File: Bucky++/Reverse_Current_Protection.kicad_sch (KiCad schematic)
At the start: 32 parts, among them IC4 LTC4372CMS8#TRPBF, IC5 LTC4372CMS8#TRPBF, IC701 LTC4372CMS8#TRPBF, IC702 LTC4372CMS8#TRPBF, Q1 ISC016N04NM7V, Q2 ISC016N04NM7V, Q3 ISC016N04NM7V, Q4 ISC016N04NM7V, Q5 ISC016N04NM7V, Q6 ISC016N04NM7V, Q7 ISC016N04NM7V, Q8 ISC016N04NM7V

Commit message: fixed issues after Pedro's review
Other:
- note removed: "Control"
- note removed: "Reverse Current Protection"
- title: (none) -> Reverse_Current_Protection
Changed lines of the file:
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@@
 	(generator_version "9.0")
 	(paper "A4")
+	(title_block
+		(title "Reverse_Current_Protection")
+	)
 	(rectangle
-		(start 19.05 161.29)
-		(end 88.9 193.04)
+		(start 144.78 99.06)
+		(end 265.43 154.94)
 		(stroke
-			(width 0)
+			(width 1)
+			(type default)
+			(color 200 200 200 1)
+		)
+		(fill
+			(type none)
+		)
+	)
+	(rectangle
+		(start 17.78 160.02)
+		(end 92.71 193.04)
+		(stroke
+			(width 1)
 			(type default)
+			(color 200 200 200 1)
 		)
 		(fill
@@
 		)
 	)
-	(text "Control\n"
+	(rectangle
+		(start 144.78 35.56)
+		(end 265.43 95.25)
+		(stroke
+			(width 1)
+			(type default)
+			(color 200 200 200 1)
+		)
+		(fill
+			(type none)
+		)
+	)
+	(rectangle
+		(start 17.78 35.56)
+		(end 138.43 95.25)
+		(stroke
+			(width 1)
+			(type default)
+			(color 200 200 200 1)
+		)
+		(fill
+			(type none)
+		)
+	)
+	(rectangle
+		(start 17.78 99.06)
+		(end 138.43 154.94)
+		(stroke
+			(width 1)
+			(type default)
+			(color 200 200 200 1)
+		)
+		(fill
+			(type none)
+		)
+	)
+	(text_box "DESIGN NOTE:\nTVS diodes are added to protect the chip and MOSFETS\n"
 		(exclude_from_sim no)
-		(at 29.21 166.116 0)
+		(at 17.78 22.86 0)
+		(size 36.83 10.16)
+		(margins 1.3525 1.3525 1.3525 1.3525)
+		(stroke
+			(width 0.8)
+			(type solid)
+			(color 200 200 200 1)
+		)
+		(fill
+			(type none)
+		)
 		(effects
 			(font
+				(face "Arial")
+				(size 1.27 1.27)
+				(color 0 0 0 1)
+			)
+			(justify left top)
+		)
+	)
+	(text_box "5V Rail"
+		(exclude_from_sim no)
+		(at 86.36 87.63 0)
+		(size 50.8 6.985)
+		(margins 1.9049 1.9049 1.9049 1.9049)
+		(stroke
+			(width -0.0001)
+			(type solid)
+		)
+		(fill
+			(type none)
+		)
+		(effects
+			(font
+				(face "Times New Roman")
 				(size 2.54 2.54)
 				(thickness 0.508)
 				(bold yes)
-				(color 18 0 255 1)
+				(color 162 22 34 1)
+			)
+			(justify bottom)
+		)
+	)
+	(text_box "DESIGN NOTE:\nISC016N04NM7V was chosen as it can hold 40V and up to 174A.\n\nWith power dissipation of over 80W, this is more than enough even for the main input as P=I2R. This Transistor can theoretically hold over 200A.\n\n"
+		(exclude_from_sim no)
+		(at 228.6 13.97 0)
+		(size 36.83 20.32)
+		(margins 1.3525 1.3525 1.3525 1.3525)
+		(stroke
+			(width 0.8)
+			(type solid)
+			(color 200 200 200 1)
+		)
+		(fill
+			(type none)
+		)
+		(effects
+			(font
+				(face "Arial")
+				(size 1.27 1.27)
+				(color 0 0 0 1)
 			)
+			(justify left top)
 		)
 	)
-	(text "Reverse Current Protection\n"
+	(text_box "12V Rail"
 		(exclude_from_sim no)
-		(at 105.41 30.226 0)
+		(at 214.63 87.63 0)
+		(size 50.8 6.985)
+		(margins 1.9049 1.9049 1.9049 1.9049)
+		(stroke
+			(width -0.0001)
+			(type solid)
+		)
+		(fill
+			(type none)
+		)
 		(effects
 			(font
+				(face "Times New Roman")
 				(size 2.54 2.54)
 				(thickness 0.508)
 				(bold yes)
-				(color 18 0 255 1)
+				(color 162 22 34 1)
 			)
+			(justify bottom)
 		)
 	)
-	(text_box "Reverse current protection to protect and shutdown the current in case of an issue in the bucks. Schematics adapted from GEODE\n"
+	(text_box "15V Rail"
 		(exclude_from_sim no)
-		(at 139.7 10.16 0)
-		(size 53.34 22.86)
-		(margins 0.9525 0.9525 0.9525 0.9525)
+		(at 86.36 147.32 0)
+		(size 50.8 6.985)
+		(margins 1.9049 1.9049 1.9049 1.9049)
 		(stroke
-			(width 0.0508)
+			(width -0.0001)
 			(type solid)
 		)
@@
 		(effects
 			(font
-				(face "Arial")
+				(face "Times New Roman")
 				(size 2.54 2.54)
-				(color 0 0 0 1)
+				(thickness 0.508)
+				(bold yes)
+				(color 162 22 34 1)
+			)
+			(justify bottom)
+		)
+	)
+	(text_box "[${#}] ${TITLE}"
+		(exclude_from_sim no)
+		(at 58.42 17.78 0)
+		(size 167.64 12.7)
+		(margins 4.4999 4.4999 4.4999 4.4999)
+		(stroke
+			(width -0.0001)
+			(type default)
+		)
+		(fill
+			(type none)
+		)
+		(effects
+			(font
+				(face "Times New Roman")
+				(size 6 6)
+				(thickness 1.2)
+				(bold yes)
+				(color 162 22 34 1)
 			)
-			(justify top)
 		)
 	)
-	(text_box "A TVS Diode is added to protect against voltage spikes after each buck output "
+	(text_box "24V Rail"
 		(exclude_from_sim no)
-		(at 19.05 17.78 0)
-		(size 53.34 15.24)
-		(margins 0.9525 0.9525 0.9525 0.9525)
+		(at 213.36 147.32 0)
+		(size 50.8 6.985)
+		(margins 1.9049 1.9049 1.9049 1.9049)
 		(stroke
-			(width 0.0508)
+			(width -0.0001)
 			(type solid)
 		)
@@
 		(effects
 			(font
-				(face "Arial")
+				(face "Times New Roman")
 				(size 2.54 2.54)
-				(color 0 0 0 1)
+				(thickness 0.508)
+				(bold yes)
+				(color 162 22 34 1)
 			)
-			(justify top)
+			(justify bottom)
 		)
 	)
@@
 			)
 		)
-		(property "Datasheet" ""
+		(property "Datasheet" "https://www.mouser.com/catalog/specsheets/Infineon_6-24-2025_DS_ISC016N04NM7V_1_0.pdf?_gl=1*jfccxs*_gcl_aw*R0NMLjE3NjI4OTA2MjIuQ2p3S0NBaUEyc3ZJQmhCLUVpd0FSV0RQamdvV0FZSHZaQkE4VjB4MTAzcEg1c1pjUjZnblZJODBjeFFlQmJZSmZpRkp3NDRhaVdNbnZCb0NZZ1lRQXZEX0J3RQ..*_gcl_au*MTExMzU0Mzc3Ni4xNzU4OTcyNDc5LjEyODI1MDMwMzEuMTc2Mjg5MDM0MS4xNzYyODkxNDE2*_ga*MTk3NDYyMTgwMy4xNzQyNDExMTU0*_ga_15W4STQT4T*czE3NjMzOTEyNDMkbzk1JGcwJHQxNzYzMzkxMjQzJGo2MCRsMCRoMA.."
 			(at 179.07 110.49 0)
 			(effects
@@
 			)
 		)
-		(property "Datasheet" ""
+		(property "Datasheet" "https://www.mouser.com/catalog/specsheets/Infineon_6-24-2025_DS_ISC016N04NM7V_1_0.pdf?_gl=1*jfccxs*_gcl_aw*R0NMLjE3NjI4OTA2MjIuQ2p3S0NBaUEyc3ZJQmhCLUVpd0FSV0RQamdvV0FZSHZaQkE4VjB4MTAzcEg1c1pjUjZnblZJODBjeFFlQmJZSmZpRkp3NDRhaVdNbnZCb0NZZ1lRQXZEX0J3RQ..*_gcl_au*MTExMzU0Mzc3Ni4xNzU4OTcyNDc5LjEyODI1MDMwMzEuMTc2Mjg5MDM0MS4xNzYyODkxNDE2*_ga*MTk3NDYyMTgwMy4xNzQyNDExMTU0*_ga_15W4STQT4T*czE3NjMzOTEyNDMkbzk1JGcwJHQxNzYzMzkxMjQzJGo2MCRsMCRoMA.."
 			(at 198.12 50.8 0)
 			(effects
@@
 			)
 		)
-		(property "Datasheet" ""
+		(property "Datasheet" "https://www.mouser.com/catalog/specsheets/Infineon_6-24-2025_DS_ISC016N04NM7V_1_0.pdf?_gl=1*jfccxs*_gcl_aw*R0NMLjE3NjI4OTA2MjIuQ2p3S0NBaUEyc3ZJQmhCLUVpd0FSV0RQamdvV0FZSHZaQkE4VjB4MTAzcEg1c1pjUjZnblZJODBjeFFlQmJZSmZpRkp3NDRhaVdNbnZCb0NZZ1lRQXZEX0J3RQ..*_gcl_au*MTExMzU0Mzc3Ni4xNzU4OTcyNDc5LjEyODI1MDMwMzEuMTc2Mjg5MDM0MS4xNzYyODkxNDE2*_ga*MTk3NDYyMTgwMy4xNzQyNDExMTU0*_ga_15W4STQT4T*czE3NjMzOTEyNDMkbzk1JGcwJHQxNzYzMzkxMjQzJGo2MCRsMCRoMA.."
 			(at 50.8 111.76 0)
 			(effects
@@
 			)
 		)
-		(property "Datasheet" ""
+		(property "Datasheet" "https://www.mouser.com/catalog/specsheets/Infineon_6-24-2025_DS_ISC016N04NM7V_1_0.pdf?_gl=1*jfccxs*_gcl_aw*R0NMLjE3NjI4OTA2MjIuQ2p3S0NBaUEyc3ZJQmhCLUVpd0FSV0RQamdvV0FZSHZaQkE4VjB4MTAzcEg1c1pjUjZnblZJODBjeFFlQmJZSmZpRkp3NDRhaVdNbnZCb0NZZ1lRQXZEX0J3RQ..*_gcl_au*MTExMzU0Mzc3Ni4xNzU4OTcyNDc5LjEyODI1MDMwMzEuMTc2Mjg5MDM0MS4xNzYyODkxNDE2*_ga*MTk3NDYyMTgwMy4xNzQyNDExMTU0*_ga_15W4STQT4T*czE3NjMzOTEyNDMkbzk1JGcwJHQxNzYzMzkxMjQzJGo2MCRsMCRoMA.."
 			(at 74.93 48.26 0)
 			(effects
@@
 			)
 		)
-		(property "Datasheet" ""
+		(property "Datasheet" "https://www.mouser.com/catalog/specsheets/Infineon_6-24-2025_DS_ISC016N04NM7V_1_0.pdf?_gl=1*jfccxs*_gcl_aw*R0NMLjE3NjI4OTA2MjIuQ2p3S0NBaUEyc3ZJQmhCLUVpd0FSV0RQamdvV0FZSHZaQkE4VjB4MTAzcEg1c1pjUjZnblZJODBjeFFlQmJZSmZpRkp3NDRhaVdNbnZCb0NZZ1lRQXZEX0J3RQ..*_gcl_au*MTExMzU0Mzc3Ni4xNzU4OTcyNDc5LjEyODI1MDMwMzEuMTc2Mjg5MDM0MS4xNzYyODkxNDE2*_ga*MTk3NDYyMTgwMy4xNzQyNDExMTU0*_ga_15W4STQT4T*czE3NjMzOTEyNDMkbzk1JGcwJHQxNzYzMzkxMjQzJGo2MCRsMCRoMA.."
 			(at 49.53 48.26 0)
 			(effects
@@
 			)
 		)
-		(property "Datasheet" ""
+		(property "Datasheet" "https://www.mouser.com/catalog/specsheets/Infineon_6-24-2025_DS_ISC016N04NM7V_1_0.pdf?_gl=1*jfccxs*_gcl_aw*R0NMLjE3NjI4OTA2MjIuQ2p3S0NBaUEyc3ZJQmhCLUVpd0FSV0RQamdvV0FZSHZaQkE4VjB4MTAzcEg1c1pjUjZnblZJODBjeFFlQmJZSmZpRkp3NDRhaVdNbnZCb0NZZ1lRQXZEX0J3RQ..*_gcl_au*MTExMzU0Mzc3Ni4xNzU4OTcyNDc5LjEyODI1MDMwMzEuMTc2Mjg5MDM0MS4xNzYyODkxNDE2*_ga*MTk3NDYyMTgwMy4xNzQyNDExMTU0*_ga_15W4STQT4T*czE3NjMzOTEyNDMkbzk1JGcwJHQxNzYzMzkxMjQzJGo2MCRsMCRoMA.."
 			(at 76.2 111.76 0)
 			(effects
@@
 			)
 		)
-		(property "Datasheet" ""
+		(property "Datasheet" "https://www.mouser.com/catalog/specsheets/Infineon_6-24-2025_DS_ISC016N04NM7V_1_0.pdf?_gl=1*jfccxs*_gcl_aw*R0NMLjE3NjI4OTA2MjIuQ2p3S0NBaUEyc3ZJQmhCLUVpd0FSV0RQamdvV0FZSHZaQkE4VjB4MTAzcEg1c1pjUjZnblZJODBjeFFlQmJZSmZpRkp3NDRhaVdNbnZCb0NZZ1lRQXZEX0J3RQ..*_gcl_au*MTExMzU0Mzc3Ni4xNzU4OTcyNDc5LjEyODI1MDMwMzEuMTc2Mjg5MDM0MS4xNzYyODkxNDE2*_ga*MTk3NDYyMTgwMy4xNzQyNDExMTU0*_ga_15W4STQT4T*czE3NjMzOTEyNDMkbzk1JGcwJHQxNzYzMzkxMjQzJGo2MCRsMCRoMA.."
 			(at 204.47 110.49 0)
 			(effects
@@
 			)
 		)
-		(property "Datasheet" ""
+		(property "Datasheet" "https://www.mouser.com/catalog/specsheets/Infineon_6-24-2025_DS_ISC016N04NM7V_1_0.pdf?_gl=1*jfccxs*_gcl_aw*R0NMLjE3NjI4OTA2MjIuQ2p3S0NBaUEyc3ZJQmhCLUVpd0FSV0RQamdvV0FZSHZaQkE4VjB4MTAzcEg1c1pjUjZnblZJODBjeFFlQmJZSmZpRkp3NDRhaVdNbnZCb0NZZ1lRQXZEX0J3RQ..*_gcl_au*MTExMzU0Mzc3Ni4xNzU4OTcyNDc5LjEyODI1MDMwMzEuMTc2Mjg5MDM0MS4xNzYyODkxNDE2*_ga*MTk3NDYyMTgwMy4xNzQyNDExMTU0*_ga_15W4STQT4T*czE3NjMzOTEyNDMkbzk1JGcwJHQxNzYzMzkxMjQzJGo2MCRsMCRoMA.."
 			(at 172.72 50.8 0)
 			(effects

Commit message: more routing
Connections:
- net 24V_source: now reaches IC5.3 (SOURCE), Q2.1 (SOURCE_1), Q2.2 (SOURCE_2), Q2.3 (SOURCE_3), Q4.1 (SOURCE_1), Q4.2 (SOURCE_2), Q4.3 (SOURCE_3)
- net 12V_source: now reaches IC702.3 (SOURCE), Q7.1 (SOURCE_1), Q7.2 (SOURCE_2), Q7.3 (SOURCE_3), Q8.1 (SOURCE_1), Q8.2 (SOURCE_2), Q8.3 (SOURCE_3)
- net 15V_source: now reaches IC4.3 (SOURCE), Q1.1 (SOURCE_1), Q1.2 (SOURCE_2), Q1.3 (SOURCE_3), Q3.1 (SOURCE_1), Q3.2 (SOURCE_2), Q3.3 (SOURCE_3)
- net 5V_source: now reaches IC701.3 (SOURCE), Q5.1 (SOURCE_1), Q5.2 (SOURCE_2), Q5.3 (SOURCE_3), Q6.1 (SOURCE_1), Q6.2 (SOURCE_2), Q6.3 (SOURCE_3)
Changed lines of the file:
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@@
+	)
+	(junction
+		(at 170.18 107.95)
+		(diameter 0)
+		(color 0 0 0 0)
 	)
 	(junction
@@
 	)
 	(junction
-		(at 173.99 108.585)
-		(diameter 0)
-		(color 0 0 0 0)
-	)
-	(junction
 		(at 167.64 46.99)
 		(diameter 0)
@@
 	)
 	(junction
-		(at 170.18 108.585)
-		(diameter 0)
-		(color 0 0 0 0)
-	)
-	(junction
 		(at 81.28 48.26)
 		(diameter 0)
@@
 	)
 	(junction
-		(at 40.64 48.26)
+		(at 40.64 45.72)
 		(diameter 0)
 		(color 0 0 0 0)
@@
 	)
 	(junction
+		(at 173.99 107.95)
+		(diameter 0)
+		(color 0 0 0 0)
+	)
+	(junction
 		(at 45.72 109.22)
 		(diameter 0)
@@
 	)
 	(junction
-		(at 44.45 48.26)
+		(at 44.45 45.72)
 		(diameter 0)
 		(color 0 0 0 0)
@@
 	(wire
 		(pts
+			(xy 173.99 107.95) (xy 173.99 128.27)
+		)
+		(stroke
+			(width 0)
+			(type default)
+		)
+	)
+	(wire
+		(pts
 			(xy 62.23 43.18) (xy 64.77 43.18)
 		)
@@
 	(wire
 		(pts
-			(xy 173.99 108.585) (xy 173.99 128.27)
-		)
-		(stroke
-			(width 0)
-			(type default)
-		)
-	)
-	(wire
-		(pts
 			(xy 215.9 128.27) (xy 173.99 128.27)
 		)
@@
 	(wire
 		(pts
-			(xy 170.18 108.585) (xy 170.18 119.38)
+			(xy 170.18 107.95) (xy 170.18 119.38)
 		)
 		(stroke
@@
 	(wire
 		(pts
+			(xy 170.18 107.95) (xy 173.99 107.95)
+		)
+		(stroke
+			(width 0)
+			(type default)
+		)
+	)
+	(wire
+		(pts
 			(xy 81.28 106.68) (xy 82.55 106.68)
 		)
@@
 	(wire
 		(pts
-			(xy 165.1 107.95) (xy 165.1 108.585)
-		)
-		(stroke
-			(width 0)
-			(type default)
-		)
-	)
-	(wire
-		(pts
 			(xy 81.28 60.96) (xy 86.36 60.96)
 		)
@@
 	(wire
 		(pts
-			(xy 31.75 48.26) (xy 40.64 48.26)
+			(xy 31.75 45.72) (xy 40.64 45.72)
 		)
 		(stroke
@@
 	(wire
 		(pts
-			(xy 162.56 107.95) (xy 165.1 107.95)
+			(xy 161.29 107.95) (xy 170.18 107.95)
 		)
 		(stroke
@@
 	(wire
 		(pts
-			(xy 44.45 48.26) (xy 44.45 68.58)
+			(xy 44.45 45.72) (xy 44.45 68.58)
 		)
 		(stroke
@@
 	(wire
 		(pts
-			(xy 173.99 105.41) (xy 173.99 108.585)
-		)
-		(stroke
-			(width 0)
-			(type default)
-		)
-	)
-	(wire
-		(pts
-			(xy 40.64 48.26) (xy 40.64 60.96)
+			(xy 173.99 105.41) (xy 173.99 107.95)
+		)
+		(stroke
+			(width 0)
+			(type default)
+		)
+	)
+	(wire
+		(pts
+			(xy 40.64 45.72) (xy 40.64 60.96)
 		)
 		(stroke
@@
 	(wire
 		(pts
-			(xy 40.64 48.26) (xy 44.45 48.26)
+			(xy 40.64 45.72) (xy 44.45 45.72)
 		)
 		(stroke
@@
 	(wire
 		(pts
-			(xy 170.18 108.585) (xy 173.99 108.585)
-		)
-		(stroke
-			(width 0)
-			(type default)
-		)
-	)
-	(wire
-		(pts
 			(xy 63.5 106.68) (xy 63.5 129.54)
 		)
@@
 	(wire
 		(pts
-			(xy 165.1 108.585) (xy 170.18 108.585)
-		)
-		(stroke
-			(width 0)
-			(type default)
-		)
-	)
-	(wire
-		(pts
 			(xy 186.69 45.72) (xy 187.96 45.72)
 		)
@@
 	(wire
 		(pts
-			(xy 44.45 43.18) (xy 44.45 48.26)
+			(xy 44.45 43.18) (xy 44.45 45.72)
 		)
 		(stroke
@@
 		)
 	)
+	(label "12V_source"
+		(at 187.96 66.04 0)
+		(effects
+			(font
+				(size 1.27 1.27)
+			)
+			(justify left bottom)
+		)
+	)
 	(label "MV24_SHDN"
 		(at 41.91 185.42 0)
@@
 		)
 	)
+	(label "5V_source"
+		(at 67.31 66.04 0)
+		(effects
+			(font
+				(size 1.27 1.27)
+			)
+			(justify left bottom)
+		)
+	)
 	(label "MV24_SHDN"
 		(at 250.19 120.65 0)
@@
 	(label "MV5_SHDN"
 		(at 120.65 60.96 0)
+		(effects
+			(font
+				(size 1.27 1.27)
+			)
+			(justify left bottom)
+		)
+	)
+	(label "24V_source"
+		(at 194.31 125.73 0)
+		(effects
+			(font
+				(size 1.27 1.27)
+			)
+			(justify left bottom)
+		)
+	)
+	(label "15V_source"
+		(at 67.31 129.54 0)
 		(effects
 			(font
@@
 	(hierarchical_label "24V_fused"
 		(shape input)
-		(at 162.56 107.95 180)
+		(at 161.29 107.95 180)
 		(effects
 			(font
@@
 	(hierarchical_label "5V_fused"
 		(shape input)
-		(at 31.75 48.26 180)
-		(effects
-			(font
+		(at 31.75 45.72 180)
+		(effects
+			(font

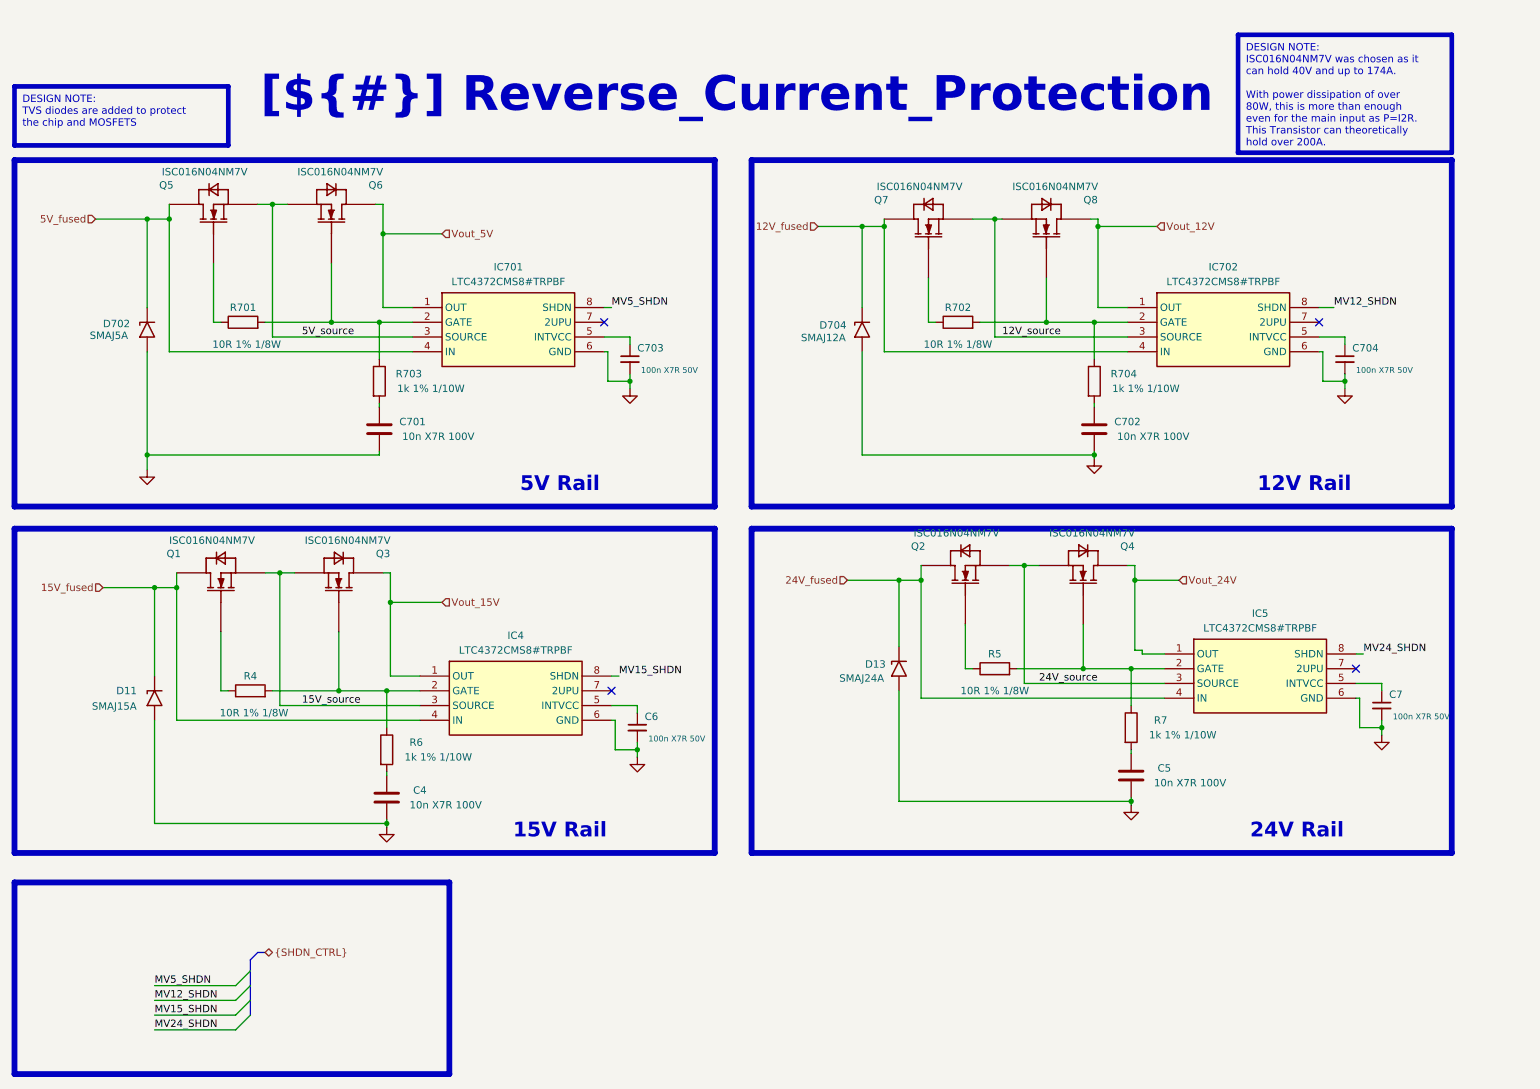
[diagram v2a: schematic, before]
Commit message: updated circuit after review. updated silkscreen
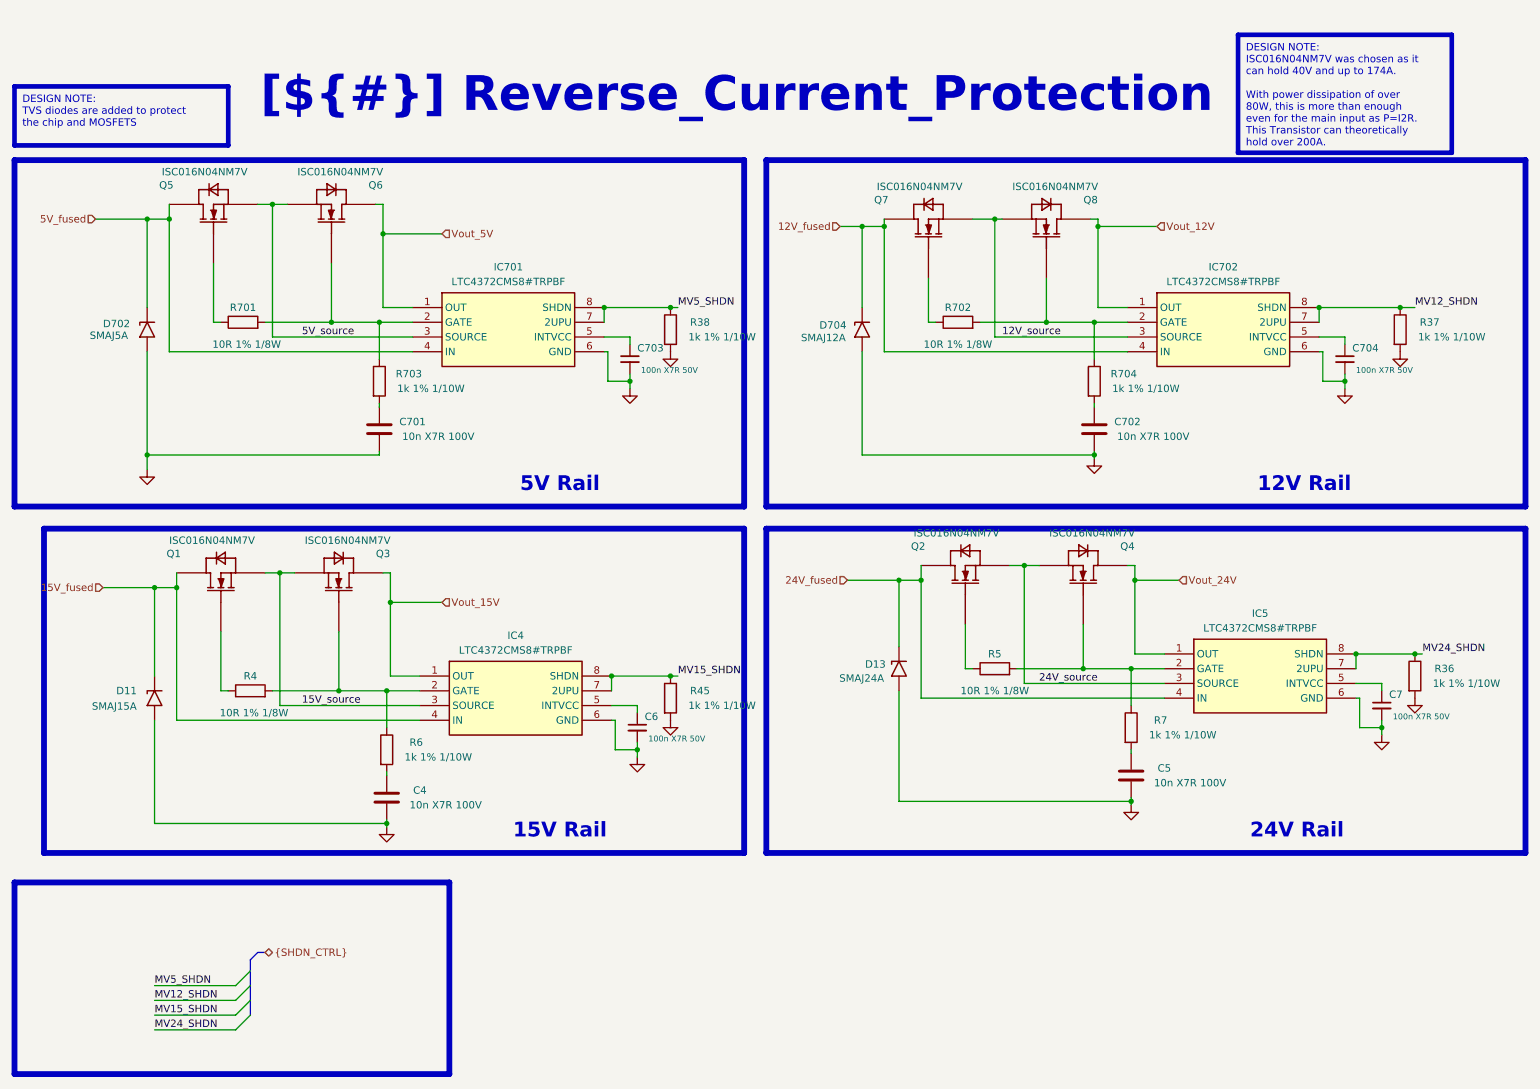
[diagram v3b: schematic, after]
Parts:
- added R36, R37, R38, R45: 1k 1% 1/10W, 0_resistor_smd:R_0603_1608_DensityHigh, symbol Device:R
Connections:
- net GND: now also R36.2, R37.2, R38.2, R45.2
- net MV12_SHDN: now also IC702.7 (2UPU), R37.1
- net MV15_SHDN: now also IC4.7 (2UPU), R45.1
- net MV24_SHDN: now also IC5.7 (2UPU), R36.1
- net MV5_SHDN: now also IC701.7 (2UPU), R38.1
- no-connect marks 4 -> 0
